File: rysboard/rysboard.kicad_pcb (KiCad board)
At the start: 2 copper layers, 70 parts, among them IC1 Integrated Circuit, J1 1x7 header, J10 1x5 header, J11 1x5 header, J12 1x5 header, J13 1x5 header, J14 1x5 header, J15 1x5 header, J16 1x5 header, J17 1x5 header, J19 1x5 header, J3 1x5 header, J8 1x5 header, J9 1x5 header, U1 SPI stepper driver, U2 SPI stepper driver, U4 DC/DC converter 3A

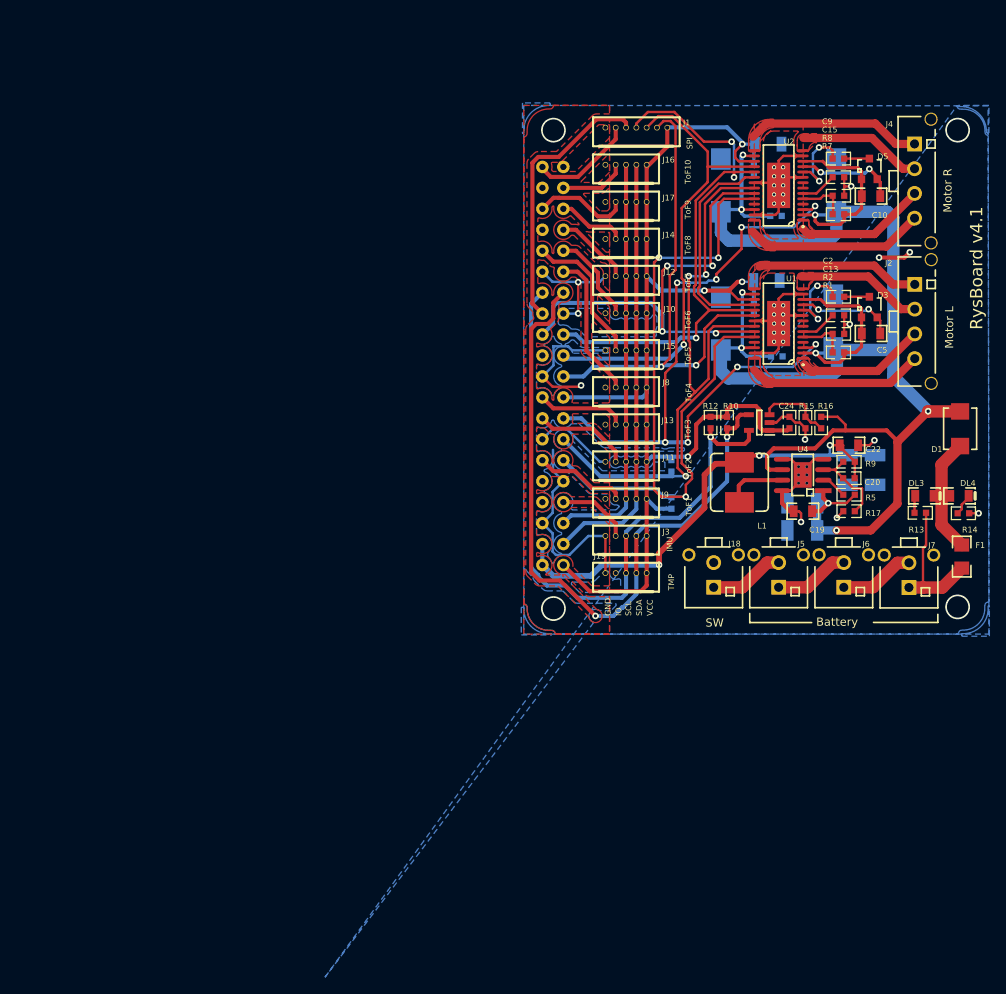
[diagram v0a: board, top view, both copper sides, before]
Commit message: rysboard: 4.2 schematic imported to pcb, initial version
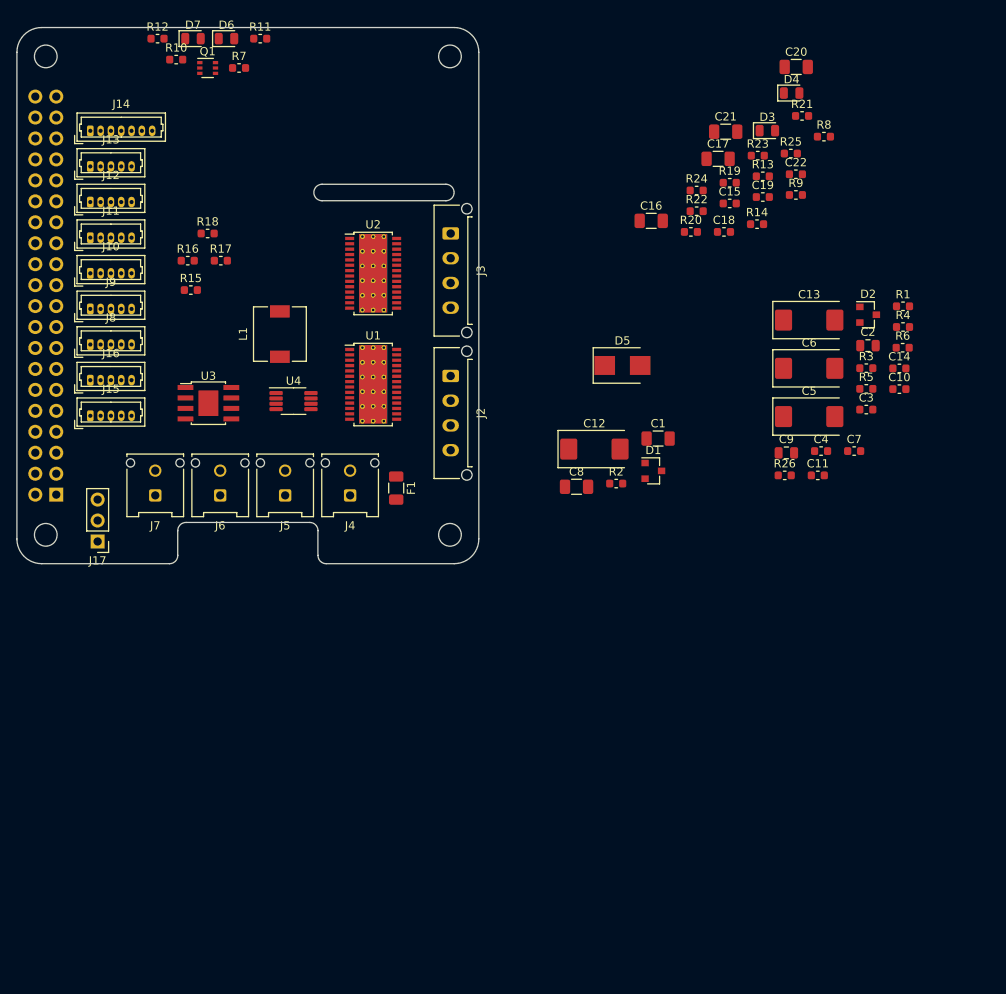
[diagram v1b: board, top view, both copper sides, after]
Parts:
- removed C23: Ceramic Capacitor, 1210_C
- removed C24: Ceramic Capacitor, 0603
- removed DL3, DL4: Light Emitting Diode, 0805_LED
- removed IC1: Integrated Circuit, SOT95P280X145-5N
- removed J18: , MICROFIT 1x2 Vertical
- removed J19: 1x5 header, PicoBlade_THT_1x5_HEADER
- added ?: , RPi_Hat:RPi_Hat_Mounting_Hole, F.Cu at (57.6, 116.5)
- added ?: , RPi_Hat:RPi_Hat_Mounting_Hole, F.Cu at (106.6, 116.5)
- added ?: , RPi_Hat:RPi_Hat_Mounting_Hole, F.Cu at (106.6, 58.5)
- added ?: , RPi_Hat:RPi_Hat_Mounting_Hole, F.Cu at (57.6, 58.5)
- added D2: BAV99, Package_TO_SOT_SMD:SOT-23, F.Cu at (157.3, 89.9)
- added D4: GREEN, LED_SMD:LED_0805_2012Metric, F.Cu at (148.0, 63.0)
- added D6: LED_GREEN, LED_SMD:LED_0805_2012Metric, F.Cu at (79.5, 56.4)
- added D7: LED_RED, LED_SMD:LED_0805_2012Metric, F.Cu at (75.4, 56.4)
- added Q1: MBT3946DW1T1, Package_TO_SOT_SMD:SOT-363_SC-70-6, F.Cu at (77.2, 59.9)
- added R11: 43R, Resistor_SMD:R_0603_1608Metric, F.Cu at (83.6, 56.4)
- added R18: 3K3, Resistor_SMD:R_0603_1608Metric, F.Cu at (77.2, 80.0)
- added R19: 15k1%, Resistor_SMD:R_0603_1608Metric, F.Cu at (140.5, 73.9)
- added R20: 10k1%, Resistor_SMD:R_0603_1608Metric, F.Cu at (135.8, 79.8)
- added R21: 36k1%, Resistor_SMD:R_0603_1608Metric, F.Cu at (149.3, 65.8)
- added R22: 10k1%, Resistor_SMD:R_0603_1608Metric, F.Cu at (136.5, 77.3)
- added R23: 56k1%, Resistor_SMD:R_0603_1608Metric, F.Cu at (143.9, 70.6)
- added R24: 10k1%, Resistor_SMD:R_0603_1608Metric, F.Cu at (136.5, 74.8)
- added R25: 10k, Resistor_SMD:R_0603_1608Metric, F.Cu at (147.9, 70.3)
- added R26: 10k, Resistor_SMD:R_0603_1608Metric, F.Cu at (147.2, 109.3)
- added R6: 10k1%, Resistor_SMD:R_0603_1608Metric, F.Cu at (161.5, 93.9)
- C1, C8: value Ceramic Capacitor -> 10u; footprint 0603 -> Capacitor_SMD:C_1206_3216Metric; moved to F.Cu
- C10, C19: value Ceramic Capacitor -> 10n; footprint 0805 -> Capacitor_SMD:C_0603_1608Metric
- C11, C18: value Ceramic Capacitor -> 100n; footprint 1210_C -> Capacitor_SMD:C_0603_1608Metric; moved to F.Cu
- C12: value Ceramic Capacitor -> 47u; footprint 1206_C -> Capacitor_Tantalum_SMD:CP_EIA-7343-31_Kemet-D; moved to F.Cu
- C13: value Ceramic Capacitor -> 47u; footprint 0603 -> Capacitor_Tantalum_SMD:CP_EIA-7343-31_Kemet-D
- C14: value Ceramic Capacitor -> 100n; footprint 1206_C -> Capacitor_SMD:C_0603_1608Metric; moved to F.Cu
- C15: value Ceramic Capacitor -> 100n; footprint 0603 -> Capacitor_SMD:C_0603_1608Metric
- C16: value Ceramic Capacitor -> 10u; footprint 1210_C -> Capacitor_SMD:C_1206_3216Metric; moved to F.Cu
- C17, C21: value Tantalum Capacitor -> 10u; footprint _C_TAN_D -> Capacitor_SMD:C_1206_3216Metric; moved to F.Cu
- C2, C9: value Ceramic Capacitor -> 220n; footprint 0603 -> Capacitor_SMD:C_0805_2012Metric
- C20: value Ceramic Capacitor -> 10u; footprint 0603 -> Capacitor_SMD:C_1206_3216Metric
- C22: value Ceramic Capacitor -> 100n; footprint 0805 -> Capacitor_SMD:C_0603_1608Metric
- C3: value Tantalum Capacitor -> 10n; footprint _C_TAN_D -> Capacitor_SMD:C_0603_1608Metric; moved to F.Cu
- C4: value Ceramic Capacitor -> 100n; footprint 0603 -> Capacitor_SMD:C_0603_1608Metric; moved to F.Cu
- C5: value Ceramic Capacitor -> 47u; footprint 0805 -> Capacitor_Tantalum_SMD:CP_EIA-7343-31_Kemet-D
- C6: value Ceramic Capacitor -> 47u; footprint 0603 -> Capacitor_Tantalum_SMD:CP_EIA-7343-31_Kemet-D; moved to F.Cu
- C7: value Tantalum Capacitor -> 100n; footprint _C_TAN_D -> Capacitor_SMD:C_0603_1608Metric; moved to F.Cu
- D1: value Schottky Diode 2A 60V -> BAV99; footprint SMB_DO-214AA -> Package_TO_SOT_SMD:SOT-23
- D3: value Charge pump diode -> RED; footprint SOT-23 -> LED_SMD:LED_0805_2012Metric
- D5: value Charge pump diode -> SK52; footprint SOT-23 -> Diode_SMD:D_SMB
- F1: value Fuse -> 2.5A; footprint 1206_R -> Fuse:Fuse_1206_3216Metric
- J1: value 1x7 header -> RPi4; footprint PicoBlade_THT_1x7_HEADER -> Connector_PinSocket_2.54mm:PinSocket_2x20_P2.54mm_Vertical; moved to B.Cu
- J10: value 1x5 header -> ToF3; footprint PicoBlade_THT_1x5_HEADER -> Connector_Molex:Molex_PicoBlade_53047-0510_1x05_P1.25mm_Vertical
- J11: value 1x5 header -> ToF4; footprint PicoBlade_THT_1x5_HEADER -> Connector_Molex:Molex_PicoBlade_53047-0510_1x05_P1.25mm_Vertical
- J12: value 1x5 header -> ToF5; footprint PicoBlade_THT_1x5_HEADER -> Connector_Molex:Molex_PicoBlade_53047-0510_1x05_P1.25mm_Vertical
- J13: value 1x5 header -> ToF6; footprint PicoBlade_THT_1x5_HEADER -> Connector_Molex:Molex_PicoBlade_53047-0510_1x05_P1.25mm_Vertical
- J14: value 1x5 header -> SPI; footprint PicoBlade_THT_1x5_HEADER -> Connector_Molex:Molex_PicoBlade_53047-0710_1x07_P1.25mm_Vertical
- J15: value 1x5 header -> Temp; footprint PicoBlade_THT_1x5_HEADER -> Connector_Molex:Molex_PicoBlade_53047-0510_1x05_P1.25mm_Vertical
- J16: value 1x5 header -> IMU; footprint PicoBlade_THT_1x5_HEADER -> Connector_Molex:Molex_PicoBlade_53047-0510_1x05_P1.25mm_Vertical
- J17: value 1x5 header -> Conn_01x03; footprint PicoBlade_THT_1x5_HEADER -> Connector_PinHeader_2.54mm:PinHeader_1x03_P2.54mm_Vertical
- J2: value (none) -> Motor L; footprint MICROFIT 4x1 Vertical -> Connector_Molex:Molex_Micro-Fit_3.0_43650-0415_1x04_P3.00mm_Vertical
- J3: value 1x5 header -> Motor R; footprint PicoBlade_THT_1x5_HEADER -> Connector_Molex:Molex_Micro-Fit_3.0_43650-0415_1x04_P3.00mm_Vertical
- J4: value (none) -> CELL3; footprint MICROFIT 4x1 Vertical -> Connector_Molex:Molex_Micro-Fit_3.0_43045-0212_2x01_P3.00mm_Vertical
- J5: value (none) -> CELL2; footprint MICROFIT 1x2 Vertical -> Connector_Molex:Molex_Micro-Fit_3.0_43045-0212_2x01_P3.00mm_Vertical
- J6: value (none) -> CELL1; footprint MICROFIT 1x2 Vertical -> Connector_Molex:Molex_Micro-Fit_3.0_43045-0212_2x01_P3.00mm_Vertical
- J7: value (none) -> SW; footprint MICROFIT 1x2 Vertical -> Connector_Molex:Molex_Micro-Fit_3.0_43045-0212_2x01_P3.00mm_Vertical
- J8: value 1x5 header -> ToF1; footprint PicoBlade_THT_1x5_HEADER -> Connector_Molex:Molex_PicoBlade_53047-0510_1x05_P1.25mm_Vertical
- J9: value 1x5 header -> ToF2; footprint PicoBlade_THT_1x5_HEADER -> Connector_Molex:Molex_PicoBlade_53047-0510_1x05_P1.25mm_Vertical
- L1: value Inductor -> 3.3uH; footprint L_HPI0624 -> Inductor_SMD:L_6.3x6.3_H3
- R1, R2, R8, R9: value Resistor -> 10k; footprint 0603_R -> Resistor_SMD:R_0603_1608Metric
- R10, R7: value Resistor -> 4K7; footprint 0603_R -> Resistor_SMD:R_0603_1608Metric
- R12: value Resistor -> 82R; footprint 0603_R -> Resistor_SMD:R_0603_1608Metric
- R13: value Resistor -> 11k1%; footprint 0603_R -> Resistor_SMD:R_0603_1608Metric
- R14: value Resistor -> 2k1%; footprint 0603_R -> Resistor_SMD:R_0603_1608Metric
- R15, R16, R17: value Resistor -> 3K3; footprint 0603_R -> Resistor_SMD:R_0603_1608Metric
- R3: value Resistor -> 27k1%; footprint 0603_R -> Resistor_SMD:R_0603_1608Metric; moved to F.Cu
- R4: value Resistor -> 10k1%; footprint 0603_R -> Resistor_SMD:R_0603_1608Metric; moved to F.Cu
- R5: value Resistor -> 27k1%; footprint 0603_R -> Resistor_SMD:R_0603_1608Metric
- U1, U2: value SPI stepper driver -> L6470; footprint ST HTSSOP-28 -> Package_SO:HTSSOP-28-1EP_4.4x9.7mm_P0.65mm_EP3.4x9.5mm_ThermalVias
- U3: value (none) -> ST1S10PHR; footprint RASPBERRYPI_S -> Package_SO:TI_SO-PowerPAD-8
- U4: value DC/DC converter 3A -> MAX11613; footprint HSOP8 -> Package_SO:MSOP-8_3x3mm_P0.65mm
- moved J7 91.7 mm to (70.9, 111.8), turned to 180 degrees
- moved J1 82.2 mm to (58.9, 111.7)
- moved R17 82.0 mm to (78.8, 83.3)
- moved R12 81.6 mm to (71.1, 56.4)
- moved J4 80.8 mm to (94.5, 111.8), turned to 180 degrees
- moved R10 80.0 mm to (73.4, 58.9)
- moved R16 79.3 mm to (74.8, 83.3)
- moved R15 76.2 mm to (75.2, 86.9)
- moved J17 76.1 mm to (63.9, 117.3), turned to 180 degrees
- moved J6 76.0 mm to (78.7, 111.8), turned to 180 degrees
- moved R7 74.8 mm to (81.0, 59.9)
- moved J13 72.1 mm to (63.0, 71.9)
- moved J11 70.4 mm to (63.0, 80.5)
- moved J16 70.0 mm to (63.0, 97.8)
- moved F1 69.1 mm to (100.1, 110.9), turned to 270 degrees
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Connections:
- net NetJ5_1 renamed /Power Supply/V_CELL1
- net NetJ6_1 renamed Net-(J6-Pad1)
- net SDI renamed /Motor Drivers/SPI_BRIDGE
- C1 pad 1: GND -> +3V3
- C1 pad 2: 3V3 -> GND
- C10 pad 1: VBOOT1 -> Net-(C10-Pad1)
- C10 pad 2: VMOT -> Net-(C10-Pad2)
- C11 pad 1: GND -> +3V3
- C11 pad 2: 5V -> GND
- C12 pad 1: GND -> Vdrive
- C12 pad 2: 3V3 -> GND
- C13 pad 1: NetC13_1 -> Vdrive
- C14 pad 1: GND -> Vdrive
- C14 pad 2: 3V3 -> GND
- C15 pad 1: NetC15_1 -> +3V3
- C16 pad 1: GND -> Vdrive
- C16 pad 2: 5V -> GND
- C18 pad 1: GND -> Vdrive
- C18 pad 2: VMOT -> GND
- C19 pad 1: GND -> +5V
- C19 pad 2: VMOT -> GND
- C2 pad 1: NetC2_1 -> Vdrive
- C2 pad 2: NetC2_2 -> Net-(C2-Pad2)
- C20 pad 1: NetC20_1 -> +5V
- C20 pad 2: 5V -> GND
- C22 pad 1: GND -> +5V
- C22 pad 2: 5V -> GND
- C4 pad 1: VMOT -> +3V3
- C5 pad 1: VBOOT0 -> Vdrive
- C5 pad 2: VMOT -> GND
- C6 pad 1: GND -> Vdrive
- C6 pad 2: 3V3 -> GND
- C8 pad 1: VMOT -> +3V3
- C9 pad 1: NetC9_1 -> Vdrive
- C9 pad 2: NetC9_2 -> Net-(C9-Pad2)
- D3 pad 1: VMOT -> Net-(D3-Pad1)
- D3 pad 2: VBOOT0 -> Net-(D3-Pad2)
- D5 pad 1: VMOT -> Vdrive
- D5 pad 2: VBOOT1 -> Net-(D3-Pad1)
- F1 pad 1: NetD1_A -> Net-(D3-Pad1)
- F1 pad 2: NetF1_2 -> /Power Supply/V_CELL3
- J1 pad 1: IRQ -> +3V3
- J1 pad 2: CE1 -> +5V
- J1 pad 3: SCLK -> /I2C1_SDA
- J1 pad 4: MISO -> +5V
- J1 pad 5: MOSI -> /I2C1_SCL
- J1 pad 6: 3V3 -> GND
- J10 pad 1: TOF1 -> Net-(J10-Pad1)
- J10 pad 2: SCL -> /TOF3_EN
- J10 pad 3: SDA -> /I2C3_SCL
- J10 pad 4: 3V3 -> /I2C3_SDA
- J11 pad 1: TOF6 -> GND
- J11 pad 2: SCL -> /TOF4_EN
- J11 pad 3: SDA -> /I2C5_SCL
- J11 pad 4: 3V3 -> /I2C5_SDA
- J12 pad 1: TOF2 -> GND
- J12 pad 2: SCL -> /TOF5_EN
- J12 pad 3: SDA -> /I2C5_SCL
- J12 pad 4: 3V3 -> /I2C5_SDA
- J13 pad 1: TOF7 -> GND
- J13 pad 2: SCL -> /TOF6_EN
- J13 pad 3: SDA -> /I2C5_SCL
- J13 pad 4: 3V3 -> /I2C5_SDA
- J14 pad 1: TOF3 -> GND
- J14 pad 2: SCL -> /SPI_IRQEXT
- J14 pad 3: SDA -> /~SPI_CS1
- J14 pad 4: 3V3 -> /SPI_CLK
- J15 pad 1: TOF8 -> GND
- J15 pad 2: SCL -> (no net)
- J15 pad 3: SDA -> /I2C1_SCL
- J15 pad 4: 3V3 -> /I2C1_SDA
- J16 pad 1: TOF4 -> GND
- J16 pad 2: SCL -> (no net)
- J16 pad 3: SDA -> /I2C1_SCL
- J16 pad 4: 3V3 -> /I2C1_SDA
- J17 pad 1: TOF9 -> GND
- J17 pad 2: SCL -> /UART_TXD
- J17 pad 3: SDA -> /UART_RXD
- J2 pad 1: NetJ2_1 -> Net-(J2-Pad1)
- J2 pad 2: NetJ2_2 -> Net-(J2-Pad2)
- J2 pad 3: NetJ2_3 -> Net-(J2-Pad3)
- J2 pad 4: NetJ2_4 -> Net-(J2-Pad4)
- J3 pad 1: OD -> Net-(J3-Pad1)
- J3 pad 2: SCL1 -> Net-(J3-Pad2)
- J3 pad 3: SDA1 -> Net-(J3-Pad3)
- J3 pad 4: 3V3 -> Net-(J3-Pad4)
- J4 pad 1: NetJ4_1 -> /Power Supply/V_CELL2
- J4 pad 2: NetJ4_2 -> /Power Supply/V_CELL3
- J5 pad 2: NetJ5_2 -> /Power Supply/V_CELL2
- J7 pad 1: NetF1_2 -> GND
- J8 pad 1: TOF0 -> Net-(J10-Pad1)
- J8 pad 2: SCL -> /TOF1_EN
- J8 pad 3: SDA -> /I2C3_SCL
- J8 pad 4: 3V3 -> /I2C3_SDA
- J9 pad 1: TOF5 -> Net-(J10-Pad1)
- J9 pad 2: SCL -> /TOF2_EN
- J9 pad 3: SDA -> /I2C3_SCL
- J9 pad 4: 3V3 -> /I2C3_SDA
- L1 pad 1: 5V -> Net-(L1-Pad1)
- L1 pad 2: NetL1_2 -> +5V
- R1 pad 1: NetR1_1 -> +3V3
- R1 pad 2: VMOT -> /~MOTOR_STBY
- R10 pad 1: SDA1 -> Net-(Q1-Pad2)
- R10 pad 2: 3V3 -> /LED2
- R12 pad 1: SCL1 -> +3V3
- R12 pad 2: 3V3 -> Net-(D7-Pad2)
- R13 pad 1: NetDL3_A -> Net-(R13-Pad1)
- R13 pad 2: NetF1_2 -> +5V
- R14 pad 1: GND -> Net-(R13-Pad1)
- R14 pad 2: NetDL4_K -> GND
- R15 pad 1: GND -> +3V3
- R15 pad 2: NetIC1_3 -> /I2C3_SDA
- R16 pad 1: NetIC1_3 -> +3V3
- R16 pad 2: VMOT -> /I2C5_SCL
- R17 pad 1: GND -> +3V3
- R17 pad 2: NetC20_1 -> /I2C5_SDA
- R2 pad 1: GND -> +3V3
- R2 pad 2: NetR1_1 -> /~MOTOR_BUSY
- R3 pad 1: BUSY -> Vdrive
- R3 pad 2: 3V3 -> Net-(R3-Pad2)
- R4 pad 1: FLAG -> Net-(R3-Pad2)
- R4 pad 2: 3V3 -> GND
- R5 pad 1: NetR5_1 -> Vdrive
- R5 pad 2: VMOT -> Net-(R5-Pad2)
- R7 pad 1: NetR7_1 -> Net-(Q1-Pad5)
- R7 pad 2: VMOT -> /LED1
- R8 pad 1: GND -> Net-(D3-Pad2)
- R8 pad 2: NetR7_1 -> /Power Supply/V_CELL3
- R9 pad 1: NetC20_1 -> Net-(D4-Pad1)
- R9 pad 2: 5V -> GND
- U1 pad 1: NetJ2_3 -> Net-(J2-Pad2)
- U1 pad 10: NetC2_2 -> Net-(C3-Pad2)
- U1 pad 11: VBOOT0 -> Net-(C2-Pad2)
- U1 pad 12: VMOT -> Vdrive
- U1 pad 14: NetJ2_2 -> Net-(J2-Pad3)
- U1 pad 15: NetJ2_1 -> Net-(J2-Pad4)
- U1 pad 16: VMOT -> Vdrive
- U1 pad 17: 3V3 -> +3V3
- U1 pad 19: SCLK -> /SPI_CLK
- U1 pad 2: VMOT -> Vdrive
- U1 pad 20: MOSI -> /SPI_MOSI
- U1 pad 22: BUSY -> /~MOTOR_BUSY
- U1 pad 23: CE0 -> /~SPI_CS0
- U1 pad 24: FLAG -> /~MOTOR_FLAG
- U1 pad 26: VMOT -> Vdrive
- U1 pad 28: NetJ2_4 -> Net-(J2-Pad1)
- U1 pad 3: STBY -> /~MOTOR_STBY
- U1 pad 4: (no net) -> +3V3
- U1 pad 5: NetR1_1 -> Net-(R3-Pad2)
- U1 pad 6: NetC13_1 -> +3V3
- U2 pad 1: NetJ4_3 -> Net-(J3-Pad2)
- U2 pad 10: NetC9_2 -> Net-(C10-Pad2)
- U2 pad 11: VBOOT1 -> Net-(C9-Pad2)
- U2 pad 12: VMOT -> Vdrive
- U2 pad 14: NetJ4_2 -> Net-(J3-Pad3)
- U2 pad 15: NetJ4_1 -> Net-(J3-Pad4)
- U2 pad 16: VMOT -> Vdrive
- U2 pad 17: 3V3 -> +3V3
- U2 pad 18: MISO -> /SPI_MISO
- U2 pad 19: SCLK -> /SPI_CLK
- U2 pad 2: VMOT -> Vdrive
- U2 pad 22: BUSY -> /~MOTOR_BUSY
- U2 pad 23: CE0 -> /~SPI_CS0
- U2 pad 24: FLAG -> /~MOTOR_FLAG
- U2 pad 26: VMOT -> Vdrive
- U2 pad 28: NetJ4_4 -> Net-(J3-Pad1)
- U2 pad 3: STBY -> /~MOTOR_STBY
- U2 pad 4: (no net) -> +3V3
- U2 pad 5: NetR7_1 -> Net-(R5-Pad2)
- U2 pad 6: NetC15_1 -> +3V3
- U3 pad 1: 3V3 -> Vdrive
- U3 pad 2: 5V -> Vdrive
- U3 pad 3: SDA -> Net-(R13-Pad1)
- U3 pad 4: 5V -> GND
- U3 pad 5: SCL -> GND
- U3 pad 6: GND -> Vdrive
- U3 pad 7: OD -> Net-(L1-Pad1)
- U3 pad 8: (no net) -> GND
- U4 pad 1: VMOT -> Net-(R19-Pad2)
- U4 pad 2: NetR5_1 -> Net-(R21-Pad2)
- U4 pad 3: NetC20_1 -> Net-(R23-Pad2)
- U4 pad 4: GND -> Net-(R25-Pad2)
- U4 pad 5: GND -> /I2C1_SDA
- U4 pad 6: VMOT -> /I2C1_SCL
- U4 pad 7: NetL1_2 -> GND
- U4 pad 8: GND -> +3V3
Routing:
- net VMOT: track 227.6 -> 0.00 mm, vias 9 -> 0
- net 3V3: track 145.2 -> 0.00 mm, vias 4 -> 0
- net GND: track 136.8 -> 0.00 mm, vias 42 -> 0
- net FLAG: track 93.8 -> 0.00 mm, vias 3 -> 0
- net STBY: track 84.1 -> 0.00 mm, vias 8 -> 0
- net SDA1: track 83.7 -> 0.00 mm, vias 2 -> 0
- net SCL1: track 80.8 -> 0.00 mm, vias 1 -> 0
- net BUSY: track 74.2 -> 0.00 mm, vias 3 -> 0
- net SCLK: track 67.8 -> 0.00 mm, vias 3 -> 0
- net MOSI: track 61.0 -> 0.00 mm, vias 2 -> 0
- net 5V: track 60.0 -> 0.00 mm, vias 3 -> 0
- net CE0: track 58.5 -> 0.00 mm, vias 4 -> 0
- net MISO: track 55.7 -> 0.00 mm, vias 1 -> 0
- net SDA: track 52.4 -> 0.00 mm
- net SCL: track 49.9 -> 0.00 mm
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- removed copper zone on B.Cu, net (none)
- removed copper zone on F.Cu, net (none)
- removed copper zone on B.Cu, net GND
- removed copper zone on F.Cu, net GND
- removed copper zone on F.Cu, net NetJ2_1
- removed copper zone on F.Cu, net NetJ2_2
- removed copper zone on F.Cu, net NetJ2_3
- removed copper zone on F.Cu, net NetJ2_4
- removed copper zone on F.Cu, net NetJ4_1
- removed copper zone on F.Cu, net NetJ4_2
- removed copper zone on F.Cu, net NetJ4_3
- removed copper zone on F.Cu, net NetJ4_4
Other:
- board outline added: 56 x 65 mm
- board text removed: "Battery"
- board text removed: "C1"
- board text removed: "C10"
- board text removed: "C11"
- board text removed: "C12"
- board text removed: "C13"
- board text removed: "C14"
- board text removed: "C15"
- board text removed: "C16"
- board text removed: "C17"
- board text removed: "C18"
- board text removed: "C19"
- board text removed: "C2"
- board text removed: "C20"
- board text removed: "C21"
- board text removed: "C22"
- board text removed: "C23"
- board text removed: "C24"
- board text removed: "C3"
- board text removed: "C4"
- board text removed: "C5"
- board text removed: "C6"
- board text removed: "C7"
- board text removed: "C8"
- board text removed: "C9"
- board text removed: "D1"
- board text removed: "D3"
- board text removed: "D5"
- board text removed: "DL3"
- board text removed: "DL4"
- board text removed: "F1"
- board text removed: "GND"
- board text removed: "IMU"
- board text removed: "IO"
- board text removed: "J1"
- board text removed: "J10"
- board text removed: "J11"
- board text removed: "J12"
- board text removed: "J13"
- board text removed: "J14"
- board text removed: "J15"
- board text removed: "J16"
- board text removed: "J17"
- board text removed: "J18"
- board text removed: "J19"
- board text removed: "J2"
- board text removed: "J3"
- board text removed: "J4"
- board text removed: "J5"
- board text removed: "J6"
- board text removed: "J7"
- board text removed: "J8"
- board text removed: "J9"
- board text removed: "L1"
- board text removed: "Motor L"
- board text removed: "Motor R"
- board text removed: "R1"
- board text removed: "R10"
- board text removed: "R12"
- board text removed: "R13"
- board text removed: "R14"
- board text removed: "R15"
- board text removed: "R16"
- board text removed: "R17"
- board text removed: "R2"
- board text removed: "R3"
- board text removed: "R4"
- board text removed: "R5"
- board text removed: "R7"
- board text removed: "R8"
- board text removed: "R9"
- board text removed: "RysBoard v4.1"
- board text removed: "SCL"
- board text removed: "SDA"
- board text removed: "SPI"
- board text removed: "SW"
- board text removed: "TMP"
- board text removed: "ToF1"
- board text removed: "ToF10"
- board text removed: "ToF2"
- board text removed: "ToF3"
- board text removed: "ToF4"
- board text removed: "ToF5"
- board text removed: "ToF6"
- board text removed: "ToF7"
- board text removed: "ToF8"
- board text removed: "ToF9"
- board text removed: "U1"
- board text removed: "U2"
- board text removed: "U4"
- board text removed: "VCC"

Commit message: rysboard v4.2: * route the whole board (TODO: ground fills, track width checks) * fix half of ToF connectors missing ground connection * swap LEDs for easier routing
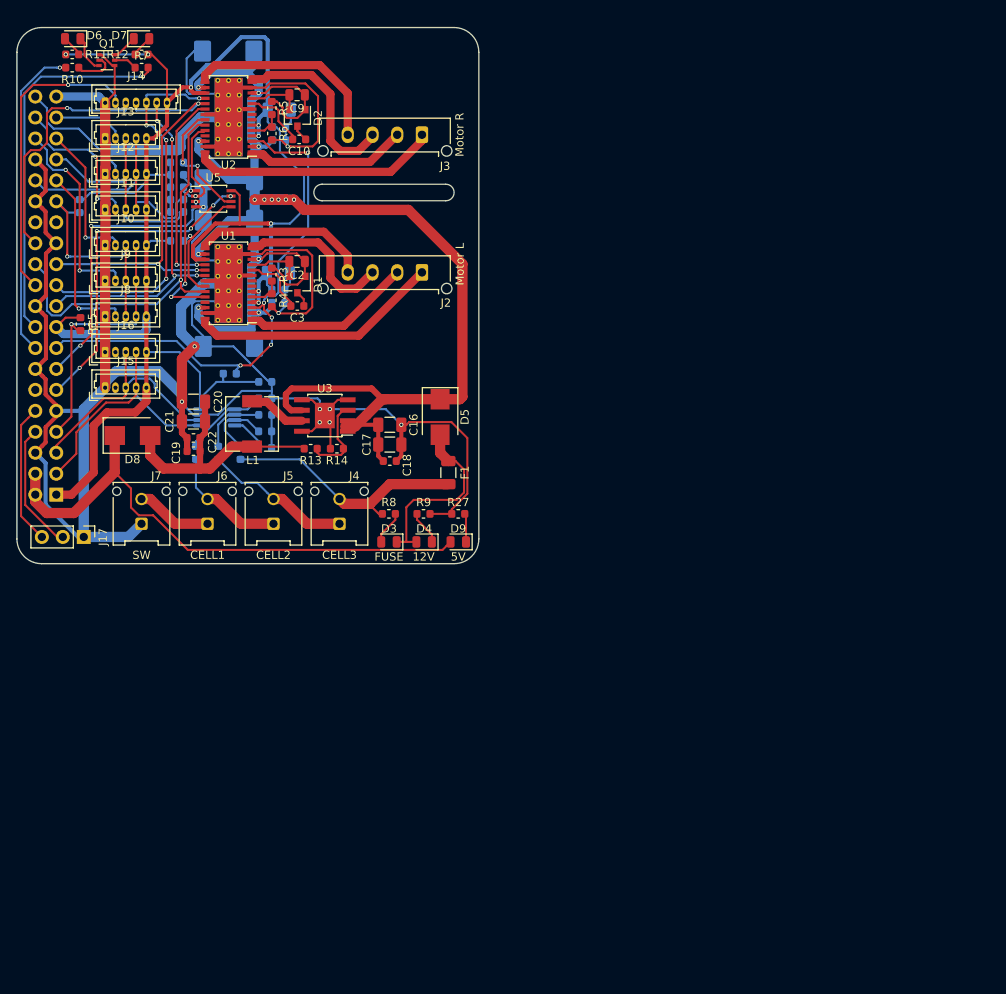
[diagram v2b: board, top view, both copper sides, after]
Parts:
- removed ? (x4): , RPi_Hat:RPi_Hat_Mounting_Hole
- added D8: SK52, Diode_SMD:D_SMB, F.Cu at (68.1, 104.5)
- added D9: GREEN, LED_SMD:LED_0805_2012Metric, F.Cu at (107.6, 117.4)
- added R27: 2k7, Resistor_SMD:R_0603_1608Metric, F.Cu at (107.6, 114.0)
- added R28: 40k, Resistor_SMD:R_0603_1608Metric, B.Cu at (73.5, 72.9)
- added R29: 40k, Resistor_SMD:R_0603_1608Metric, B.Cu at (73.5, 74.4)
- added U5: 74AHC2G00, Package_SO:TSSOP-8_3x3mm_P0.65mm, F.Cu at (77.9, 75.8)
- C1, C11, C12, C13, C14, C15, C4, C5, C6, C7, C8, R16, R17, R18, R19, R20, R21, R22, R23, R24, R25, U4: moved to B.Cu
- R1, R2, R26: value 10k -> 40k; moved to B.Cu
- R13: value 11k1% -> 130k1%
- R14: value 2k1% -> 22k1%
- moved C20 83.6 mm to (75.5, 100.4), turned to 180 degrees
- moved R26 82.9 mm to (73.5, 71.4)
- moved R1 82.0 mm to (79.9, 97.0)
- moved R21 81.7 mm to (78.5, 106.6), turned to 90 degrees
- moved R6 80.8 mm to (85.0, 67.9), turned to 270 degrees
- moved C14 80.1 mm to (85.9, 68.7)
- moved C22 79.7 mm to (75.5, 104.8), turned to 180 degrees
- moved R5 79.7 mm to (85.0, 64.8), turned to 270 degrees
- moved C10 78.8 mm to (88.3, 68.6), turned to 180 degrees
- moved C11 77.8 mm to (85.9, 67.1)
- moved C13 77.6 mm to (79.7, 57.9), turned to 180 degrees
- moved R4 76.6 mm to (85.0, 88.1), turned to 270 degrees
- moved C19 75.6 mm to (75.5, 106.4), turned to 180 degrees
- moved C9 73.5 mm to (88.1, 63.2), turned to 180 degrees
- moved C21 73.5 mm to (75.5, 102.8), turned to 180 degrees
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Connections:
- C19 pad 1: +5V -> Net-(C19-Pad1)
- C20 pad 1: +5V -> Net-(C19-Pad1)
- C21 pad 1: +5V -> Net-(C19-Pad1)
- C22 pad 1: +5V -> Net-(C19-Pad1)
- J1 pad 11: /~MOTOR_FLAG -> /MOTOR_FLAG
- J1 pad 13: /~MOTOR_BUSY -> /MOTOR_BUSY
- J10 pad 1: Net-(J10-Pad1) -> GND
- J8 pad 1: Net-(J10-Pad1) -> GND
- J9 pad 1: Net-(J10-Pad1) -> GND
- L1 pad 2: +5V -> Net-(C19-Pad1)
- R10 pad 2: /LED2 -> /LED1
- R13 pad 2: +5V -> Net-(C19-Pad1)
- R2 pad 2: /~MOTOR_BUSY -> /Motor Drivers/~BUSY_1
- R26 pad 2: /~MOTOR_BUSY -> /Motor Drivers/~BUSY_2
- R7 pad 2: /LED1 -> /LED2
- U1 pad 22: /~MOTOR_BUSY -> /Motor Drivers/~BUSY_1
- U1 pad 24: /~MOTOR_FLAG -> /Motor Drivers/~FLAG_1
- U2 pad 22: /~MOTOR_BUSY -> /Motor Drivers/~BUSY_2
- U2 pad 24: /~MOTOR_FLAG -> /Motor Drivers/~FLAG_2
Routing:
- net GND: track 0.00 -> 409.4 mm, vias 0 -> 10
- net +3V3: track 0.00 -> 216.6 mm, vias 0 -> 8
- net Vdrive: track 0.00 -> 204.1 mm, vias 0 -> 14
- net +5V: track 0.00 -> 66.5 mm
- net /~MOTOR_STBY: track 0.00 -> 65.4 mm, vias 0 -> 5
- net /SPI_CLK: track 0.00 -> 49.7 mm, vias 0 -> 3
- net /~SPI_CS0: track 0.00 -> 49.0 mm, vias 0 -> 1
- net /LED2: track 0.00 -> 45.5 mm, vias 0 -> 1
- net /SPI_MISO: track 0.00 -> 45.3 mm, vias 0 -> 4
- net /SPI_MOSI: track 0.00 -> 41.6 mm, vias 0 -> 4
- net /MOTOR_FLAG: track 0.00 -> 39.5 mm, vias 0 -> 5
- net /LED1: track 0.00 -> 38.5 mm, vias 0 -> 1
- net /SPI_IRQEXT: track 0.00 -> 37.0 mm, vias 0 -> 1
- net /MOTOR_BUSY: track 0.00 -> 34.2 mm, vias 0 -> 3
- net /I2C3_SDA: track 0.00 -> 32.6 mm, vias 0 -> 1
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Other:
- outline, holes or cut-outs redrawn
- net class Default: clearance 0.4 -> 0.15; trace_width 0.254 -> 0.25; via_dia 0.889 -> 0.5; via_drill 0.635 -> 0.3
- net class Power 2.5A added: clearance 0.25, trace_width 1, via_dia 1, via_drill 0.5
- net class Power 2A added: clearance 0.25, trace_width 0.75, via_dia 0.75, via_drill 0.4
- net class Power 3A added: clearance 0.4, trace_width 1.25, via_dia 1.25, via_drill 0.7
- net class Power output added: clearance 0.2, trace_width 1, via_dia 1, via_drill 0.5
- net class Power small added: clearance 0.2, trace_width 0.5, via_dia 0.5, via_drill 0.3
- rule trace_clearance: 0.4 -> 0.15
- rule trace_min: 0.254 -> 0.1
- rule via_min_drill: 0.508 -> 0.2
- rule via_min_size: 0.889 -> 0.5

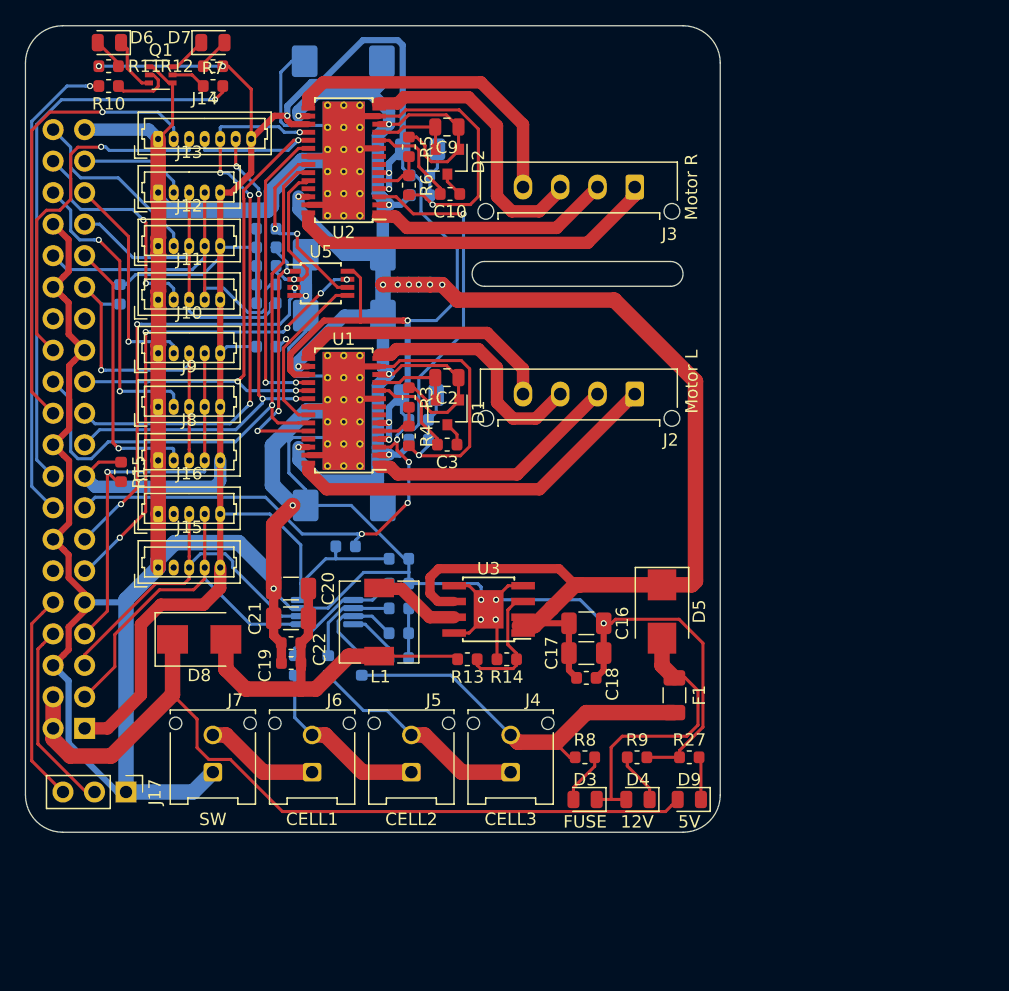
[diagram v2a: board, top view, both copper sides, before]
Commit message: rysboard v4.2: adjust placement of text on pcb front side silkscreen
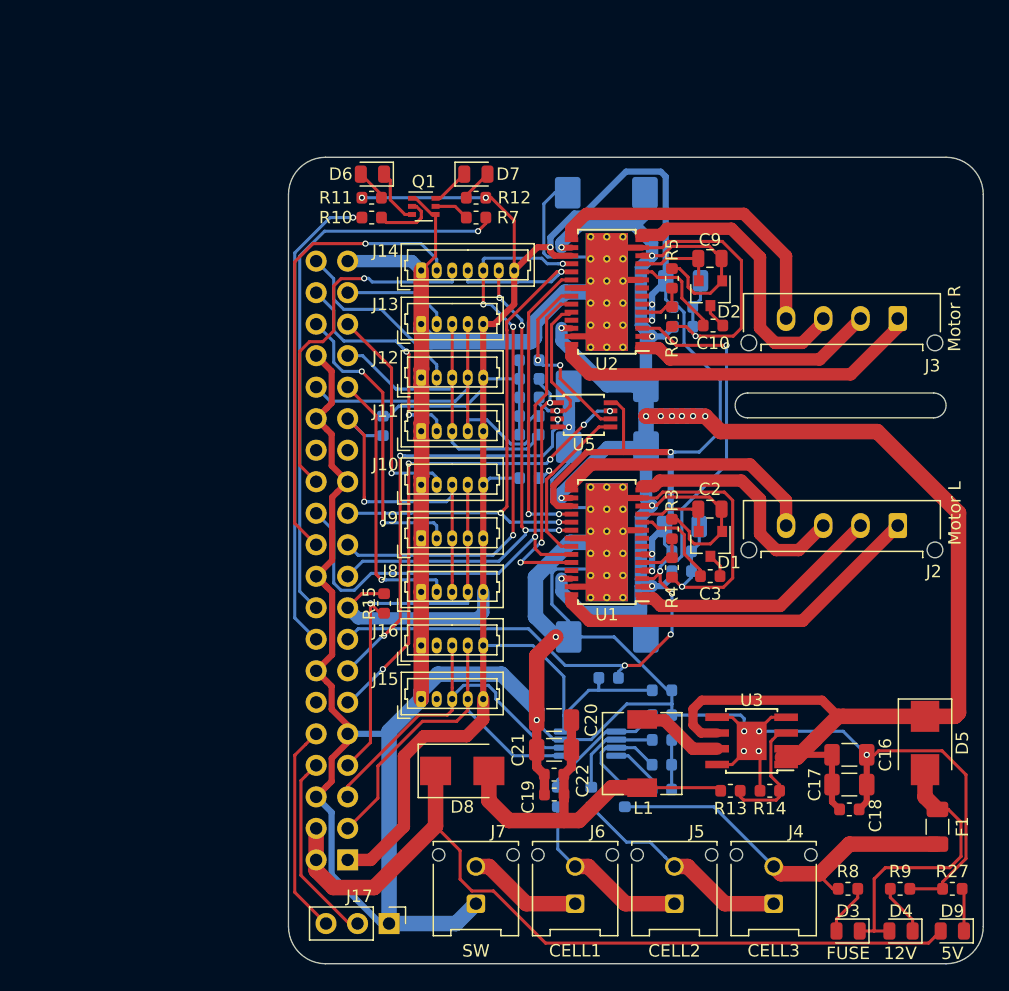
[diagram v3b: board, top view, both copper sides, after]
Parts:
- moved D9 23.7 mm to (128.8, 128.0)
- moved R27 23.7 mm to (128.8, 124.6)
- moved C1 23.7 mm to (107.0, 95.4)
- moved C10 23.7 mm to (109.5, 79.2)
- moved C11 23.7 mm to (107.1, 77.7)
- moved C17 23.7 mm to (120.5, 116.2)
- moved C18 23.7 mm to (120.5, 118.2)
- moved C21 23.7 mm to (96.7, 113.4)
- moved C22 23.7 mm to (96.7, 115.4)
- moved C4 23.7 mm to (107.0, 97.4)
- moved J11 23.7 mm to (86.0, 87.7)
- moved J12 23.7 mm to (86.0, 83.4)
- moved J15 23.7 mm to (86.0, 109.3)
- moved J17 23.7 mm to (83.4, 127.4)
- moved J2 23.7 mm to (124.4, 95.3)
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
